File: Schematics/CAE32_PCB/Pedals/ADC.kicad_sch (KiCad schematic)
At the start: 29 parts, among them J10 Conn_01x03_Female, J11 Conn_01x03_Female, J13 Conn_01x03_Female, J14 Conn_01x03_Female, J5 Conn_01x03_Female, J6 Conn_01x03_Female, J7 Conn_01x03_Female, J9 Conn_01x03_Female, U2 REF3033, U3 ADC128S022

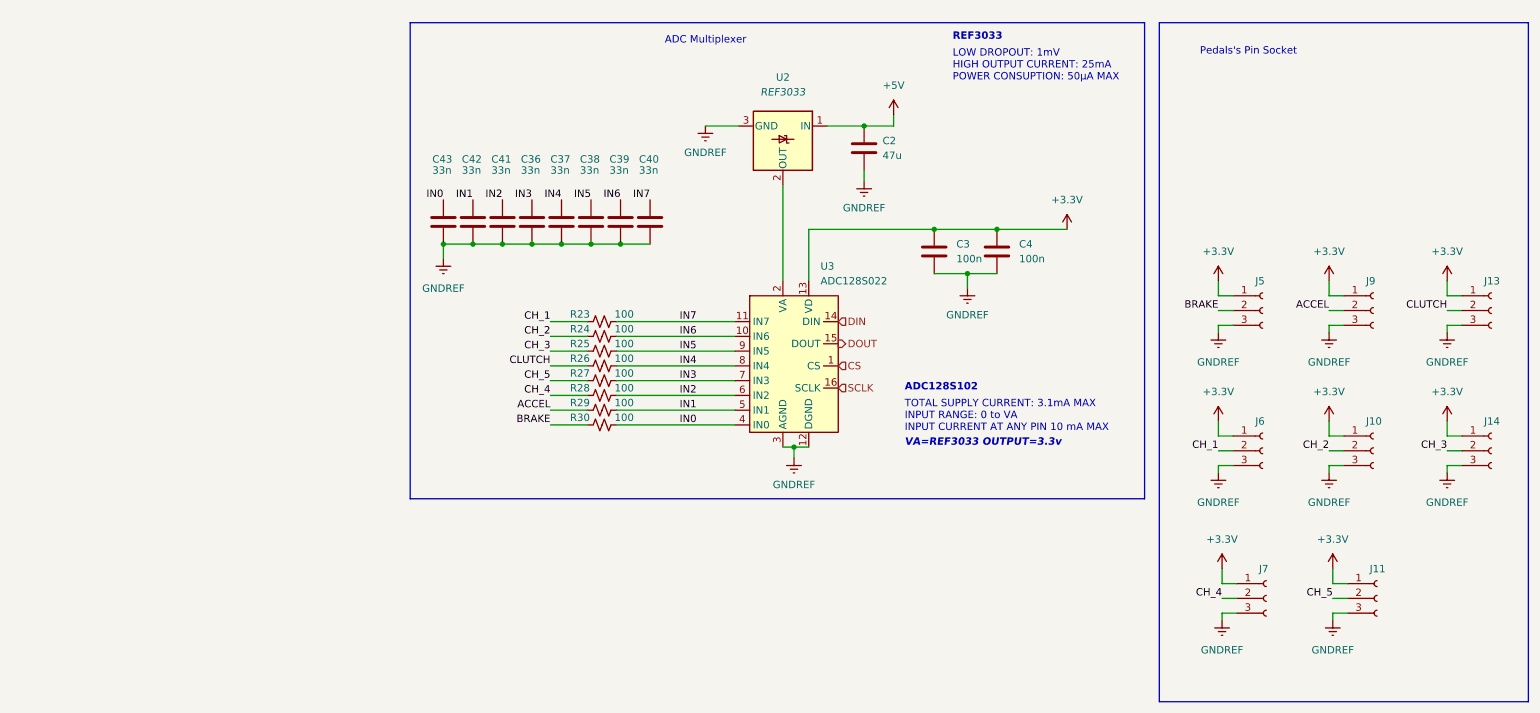
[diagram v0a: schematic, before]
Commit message: updated: Pcb design, fixed plane grounds and minor improvements, added stlink connector, updated BOM with the current market stock
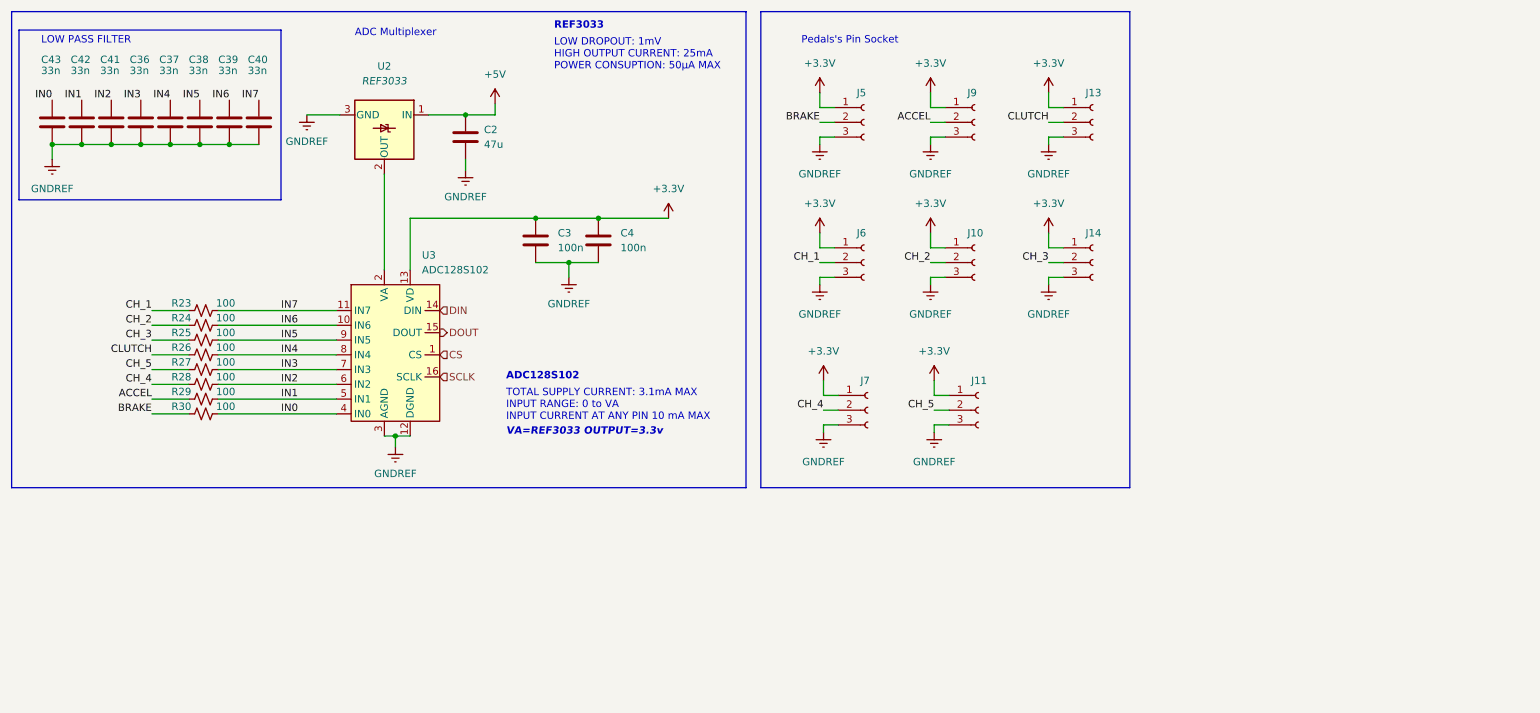
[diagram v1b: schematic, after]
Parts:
- C3, C4: Item c1591 -> C66501; LCSC_PART c1591 -> C66501; Vendor c1591 -> C66501
- C36, C37, C38, C39, C40, C41, C42, C43: Item C2929162 -> C21117; LCSC_PART C2929162 -> C21117; Vendor C2929162 -> C21117
- U3: value ADC128S022 -> ADC128S102; LCSC_PART C180424 -> C179666; Vendor C180424 -> C179666
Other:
- note added: "LOW PASS FILTER"
- moved on the sheet: C2, C3, C36, C37, C38, C39, C4, C40, C41, C42, C43, J10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

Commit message: fixed: SPI route
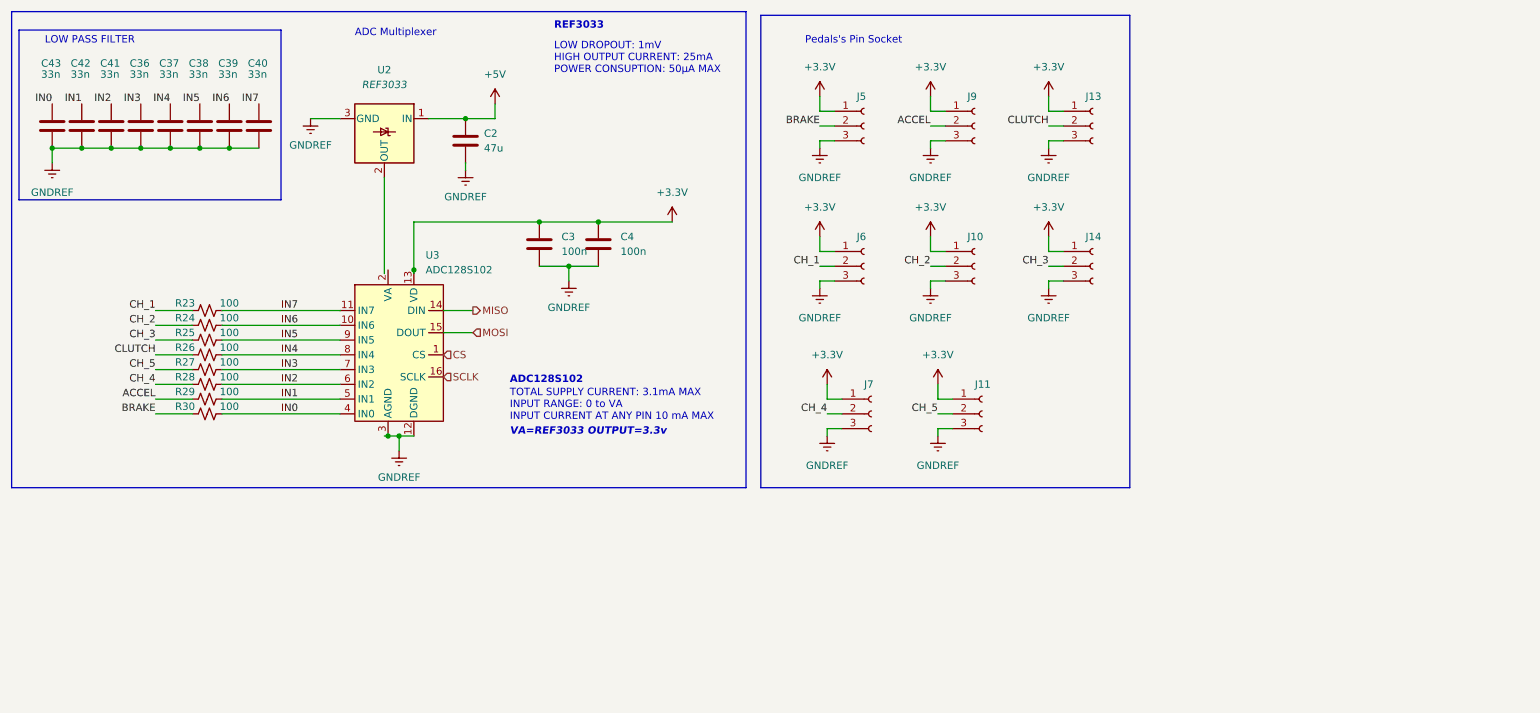
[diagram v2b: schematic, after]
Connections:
- net at U2.2 (OUT): no longer U3.2 (VA)
- net DIN renamed MISO
- net DOUT renamed MOSI
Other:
- moved on the sheet: C2, C3, C36, C37, C38, C39, C4, C40, C41, C42, C43, J10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

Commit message: fixed: SPI route and updated kicad versions in schematic and pcb design
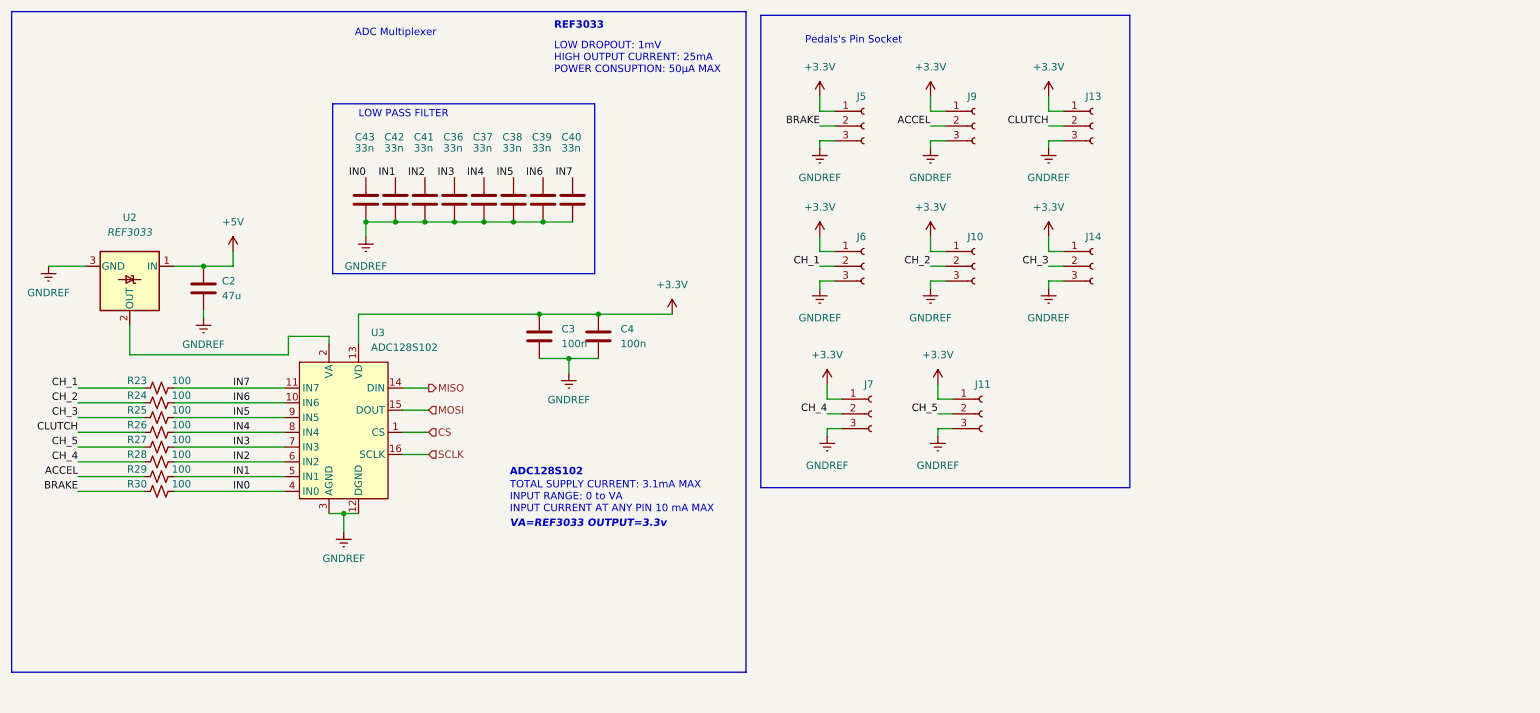
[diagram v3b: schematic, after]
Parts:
- U3: Item C179666 -> (none); LCSC_PART C179666 -> (none); Qty 1 -> (none); Vendor C179666 -> (none)
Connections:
- net at U2.2 (OUT): now also U3.2 (VA)
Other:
- moved on the sheet: C2, C3, C36, C37, C38, C39, C4, C40, C41, C42, C43, R23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
